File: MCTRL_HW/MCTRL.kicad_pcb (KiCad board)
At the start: 2 copper layers, 70 x 50 mm, 21 parts, among them J1 393570004, J2 393570004, J3 393570004, U1 IR2110, U2 IR2110, U3 IPD70R360P7SAUMA1, U4 IPD70R360P7SAUMA1, U5 IPD70R360P7SAUMA1, U6 IPD70R360P7SAUMA1

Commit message: Unfinished PCB
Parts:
- added C2: 22u, MCTRL:EEEFK1H220P, F.Cu at (151.0, 120.6)
- added C6: 22u, MCTRL:EEEFK1H220P, F.Cu at (151.0, 94.6)
- added D1: UF4007, Diode_THT:D_DO-15_P12.70mm_Horizontal, F.Cu at (159.0, 109.0)
- added D4: UF4007, Diode_THT:D_DO-15_P12.70mm_Horizontal, F.Cu at (159.0, 88.7)
- C1, C4: footprint Capacitor_THT:C_Disc_D5.0mm_W2.5mm_P5.00mm -> MCTRL:UUP1H0R1MCL1GS
- C3, C5: footprint Capacitor_THT:C_Disc_D5.0mm_W2.5mm_P5.00mm -> MCTRL:UWP1HR22MCL1GB
- U3, U4, U5, U6: value IPD70R360P7SAUMA1 -> IPAN60R125PFD7SXKSA1; footprint MCTRL:IPD70R360P7SAUMA1 -> MCTRL:IPAN60R125PFD7SXKSA1
- moved C4 106.3 mm to (131.5, 92.0), turned to -90 degrees
- moved C1 102.5 mm to (131.5, 118.0), turned to -90 degrees
- moved C5 91.2 mm to (151.0, 86.5), turned to -90 degrees
- moved U2 85.5 mm to (143.6, 99.7), turned to 180 degrees
- moved C3 83.0 mm to (151.0, 112.5), turned to -90 degrees
- moved U1 81.3 mm to (143.6, 125.7), turned to 180 degrees
- moved J3 80.4 mm to (124.0, 112.5), turned to -90 degrees
- moved J2 79.5 mm to (124.0, 87.5), turned to -90 degrees
- moved U6 75.7 mm to (172.0, 100.5), turned to 90 degrees
- moved R4 67.4 mm to (163.5, 87.5)
- moved U4 65.3 mm to (172.0, 114.5), turned to 90 degrees
- moved U5 55.2 mm to (185.0, 100.5), turned to 90 degrees
- moved D6 54.3 mm to (163.5, 83.5)
- moved R3 51.3 mm to (180.3, 87.5)
- moved U3 47.8 mm to (185.0, 114.5), turned to 90 degrees
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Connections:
- J2 pad 1: +3.3V -> +10V
- J2 pad 2: +10V -> +3.3V
- J3 pad 1: Net-(U1-HIN) -> Net-(U2-LIN)
- J3 pad 2: Net-(U1-LIN) -> Net-(U2-HIN)
- J3 pad 3: Net-(U2-HIN) -> Net-(U1-HIN)
- J3 pad 4: Net-(U2-LIN) -> Net-(U1-LIN)
- U1 pad 1: Net-(D3-K) -> Net-(D3-A)
- U4 pad 1: Net-(D3-A) -> Net-(D3-K)
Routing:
- net COM: track 0.00 -> 113.9 mm
- net +10V: track 0.00 -> 108.9 mm
- net Net-(U2-VS): track 0.00 -> 79.5 mm
- net Net-(D2-K): track 0.00 -> 65.9 mm
- net VSS: track 0.00 -> 65.6 mm
- net Net-(U1-VS): track 0.00 -> 57.2 mm
- net +3.3V: track 0.00 -> 51.1 mm
- net Net-(D6-K): track 0.00 -> 49.5 mm
- net Net-(D5-K): track 0.00 -> 43.2 mm
- net Net-(U1-SD): track 0.00 -> 43.2 mm
- net Net-(U2-HIN): track 0.00 -> 35.9 mm, vias 0 -> 1
- net +VDD: track 0.00 -> 32.2 mm
- net Net-(U2-LIN): track 0.00 -> 27.0 mm, vias 0 -> 1
- net Net-(D3-A): track 0.00 -> 24.4 mm
- net Net-(D5-A): track 0.00 -> 22.2 mm
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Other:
- board size 70 x 50 mm -> 80 x 50 mm

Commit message: Finished first proto
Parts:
- moved C2 2.00 mm to (151.0, 122.6), turned to -90 degrees
- moved C6 2.00 mm to (151.0, 96.6), turned to -90 degrees
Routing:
- net COM: track 113.9 -> 137.5 mm
- net Net-(U1-HIN): track 13.6 -> 34.7 mm
- net Net-(U1-LIN): track 12.9 -> 34.1 mm
- net Net-(U2-LIN): track 27.0 -> 34.3 mm, vias 1 -> 0
- net +10V: track 108.9 -> 106.4 mm
- net Net-(U2-HIN): track 35.9 -> 34.4 mm, vias 1 -> 0
- net Net-(D4-K): track 18.9 -> 20.0 mm
- net Net-(D1-K): track 17.6 -> 18.3 mm
- net Net-(U1-SD): track 43.2 -> 42.8 mm, vias 0 -> 1

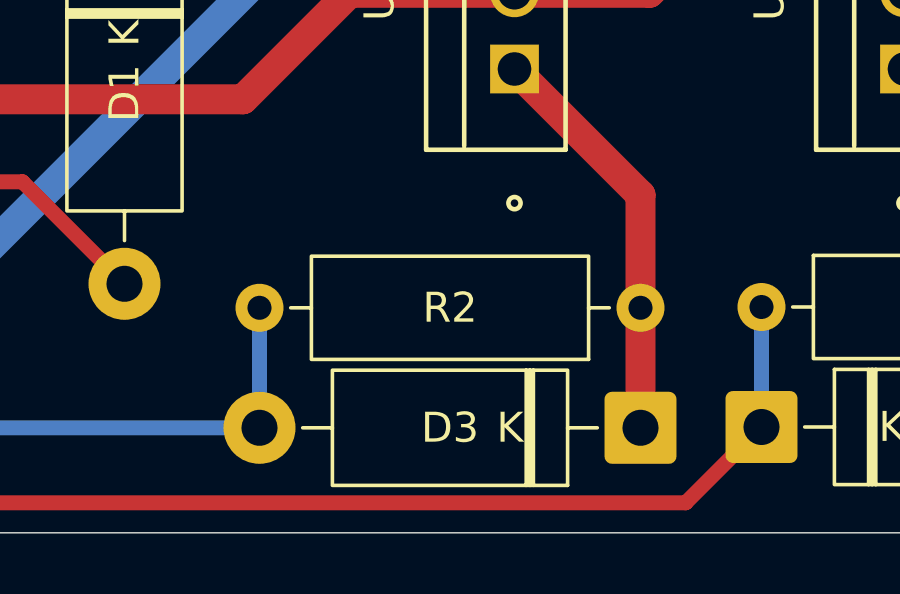
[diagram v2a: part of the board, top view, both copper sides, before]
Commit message: Fixed diode direction
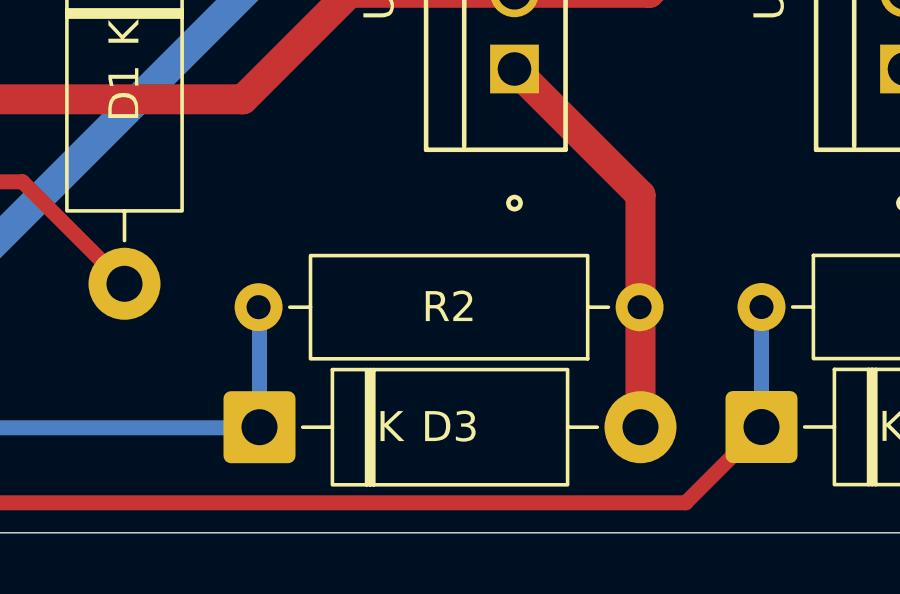
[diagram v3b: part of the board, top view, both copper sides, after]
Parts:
- moved D3 12.7 mm to (163.5, 126.5), turned to 0 degrees
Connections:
- R2 pad 1: Net-(D3-K) -> Net-(D3-A)
- R2 pad 2: Net-(D3-A) -> Net-(D3-K)
- U1 pad 1: Net-(D3-A) -> Net-(D3-K)
- U4 pad 1: Net-(D3-K) -> Net-(D3-A)
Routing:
- net Net-(D3-A): track 24.4 -> 13.7 mm
- net Net-(D3-K): track 13.7 -> 24.4 mm
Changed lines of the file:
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@@
 	(footprint "Resistor_THT:R_Axial_DIN0309_L9.0mm_D3.2mm_P12.70mm_Horizontal"
 		(layer "F.Cu")
-		(at 176.2 122.5 180)
+		(at 176.17 122.48 180)
 		(descr "Resistor, Axial_DIN0309 series, Axial, Horizontal, pin pitch=12.7mm, 0.5W = 1/2W, length*diameter=9*3.2mm^2, http://cdn-reichelt.de/documents/datenblatt/B400/1_4W%23YAG.pdf")
 		(tags "Resistor Axial_DIN0309 series Axial Horizontal pin pitch 12.7mm 0.5W = 1/2W length 9mm diameter 3.2mm")
@@
 			(layers "*.Cu" "*.Mask")
 			(remove_unused_layers no)
-			(net "Net-(D3-K)")
+			(net "Net-(D3-A)")
 			(pintype "passive")
 		)
@@
 			(layers "*.Cu" "*.Mask")
 			(remove_unused_layers no)
-			(net "Net-(D3-A)")
+			(net "Net-(D3-K)")
 			(pintype "passive")
 		)
@@
 	(footprint "Diode_THT:D_DO-15_P12.70mm_Horizontal"
 		(layer "F.Cu")
-		(at 176.2 126.5 180)
+		(at 163.5 126.48)
 		(descr "Diode, DO-15 series, Axial, Horizontal, pin pitch=12.7mm, length*diameter=7.6*3.6mm^2, http://www.diodes.com/_files/packages/DO-15.pdf")
 		(tags "Diode DO-15 series Axial Horizontal pin pitch 12.7mm  length 7.6mm diameter 3.6mm")
@@
 		)
 		(property "Sim.Device" "D"
-			(at 0 0 180)
+			(at 0 0 0)
 			(unlocked yes)
 			(layer "F.Fab")
@@
 		)
 		(property "Sim.Pins" "1=K 2=A"
-			(at 0 0 180)
+			(at 0 0 0)
 			(unlocked yes)
 			(layer "F.Fab")
@@
 		(duplicate_pad_numbers_are_jumpers no)
 		(fp_line
-			(start 11.26 0)
-			(end 10.27 0)
+			(start 1.44 0)
+			(end 2.43 0)
 			(stroke
 				(width 0.12)
@@
 		)
 		(fp_line
-			(start 3.81 -1.92)
-			(end 3.81 1.92)
+			(start 3.57 -1.92)
+			(end 3.57 1.92)
 			(stroke
 				(width 0.12)
@@
 		)
 		(fp_line
-			(start 3.57 -1.92)
-			(end 3.57 1.92)
+			(start 3.81 -1.92)
+			(end 3.81 1.92)
 			(stroke
 				(width 0.12)
@@
 		)
 		(fp_line
-			(start 1.44 0)
-			(end 2.43 0)
+			(start 11.26 0)
+			(end 10.27 0)
 			(stroke
 				(width 0.12)
@@
 		)
 		(fp_line
-			(start 12.7 0)
-			(end 10.15 0)
+			(start 0 0)
+			(end 2.55 0)
 			(stroke
 				(width 0.1)
@@
 		)
 		(fp_line
-			(start 3.79 -1.8)
-			(end 3.79 1.8)
+			(start 3.59 -1.8)
+			(end 3.59 1.8)
 			(stroke
 				(width 0.1)
@@
 		)
 		(fp_line
-			(start 3.59 -1.8)
-			(end 3.59 1.8)
+			(start 3.79 -1.8)
+			(end 3.79 1.8)
 			(stroke
 				(width 0.1)
@@
 		)
 		(fp_line
-			(start 0 0)
-			(end 2.55 0)
+			(start 12.7 0)
+			(end 10.15 0)
 			(stroke
 				(width 0.1)
@@
 			)
 		)
-		(fp_text user "${REFERENCE}"
-			(at 6.92 0 0)
+		(fp_text user "K"
+			(at 0 -2.2 0)
 			(layer "F.Fab")
 			(effects
@@
 			)
 		)
-		(fp_text user "K"
-			(at 0 -2.2 0)
+		(fp_text user "${REFERENCE}"
+			(at 6.92 0 0)
 			(layer "F.Fab")
 			(effects
@@
 		)
 		(pad "1" thru_hole roundrect
-			(at 0 0 180)
+			(at 0 0)
 			(size 2.4 2.4)
 			(drill 1.2)
@@
 		)
 		(pad "2" thru_hole circle
-			(at 12.7 0 180)
+			(at 12.7 0)
 			(size 2.4 2.4)
 			(drill 1.2)
@@
 			(remove_unused_layers no)
 			(roundrect_rratio 0.15625)
-			(net "Net-(D3-A)")
+			(net "Net-(D3-K)")
 			(pinfunction "LO_1")
 			(pintype "output")
@@
 			(layers "*.Cu" "*.Mask")
 			(remove_unused_layers no)
-			(net "Net-(D3-K)")
+			(net "Net-(D3-A)")
 			(pinfunction "GATE_1")
 			(pintype "unspecified")
@@
 	)
 	(segment
-		(start 176.2 122.5)
-		(end 176.2 118.74)
-		(width 1)
-		(layer "F.Cu")
-		(net "Net-(D3-K)")
-	)
-	(segment
-		(start 176.2 118.74)
-		(end 172 114.54)
-		(width 1)
-		(layer "F.Cu")
-		(net "Net-(D3-K)")
-	)
-	(segment
-		(start 176.2 126.5)
-		(end 176.2 122.5)
-		(width 1)
-		(layer "F.Cu")
-		(net "Net-(D3-K)")
-	)
-	(segment
 		(start 163.439998 126.439998)
 		(end 163.5 126.5)
 		(width 0.5)
 		(layer "F.Cu")
-		(net "Net-(D3-A)")
+		(net "Net-(D3-K)")
 	)
 	(segment
@@
 		(width 0.5)
 		(layer "B.Cu")
-		(net "Net-(D3-A)")
+		(net "Net-(D3-K)")
 	)
 	(segment
@@
 		(width 0.5)
 		(layer "B.Cu")
-		(net "Net-(D3-A)")
+		(net "Net-(D3-K)")
 	)
 	(segment
@@
 		(width 0.5)
 		(layer "B.Cu")
+		(net "Net-(D3-K)")
+	)
+	(segment
+		(start 176.2 118.74)
+		(end 172 114.54)
+		(width 1)
+		(layer "F.Cu")
+		(net "Net-(D3-A)")
+	)
+	(segment
+		(start 176.2 126.48)
+		(end 176.2 118.74)
+		(width 1)
+		(layer "F.Cu")
 		(net "Net-(D3-A)")
 	)
